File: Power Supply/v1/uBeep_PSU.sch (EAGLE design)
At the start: 1 part, among them U1 RAC10-12DK/277

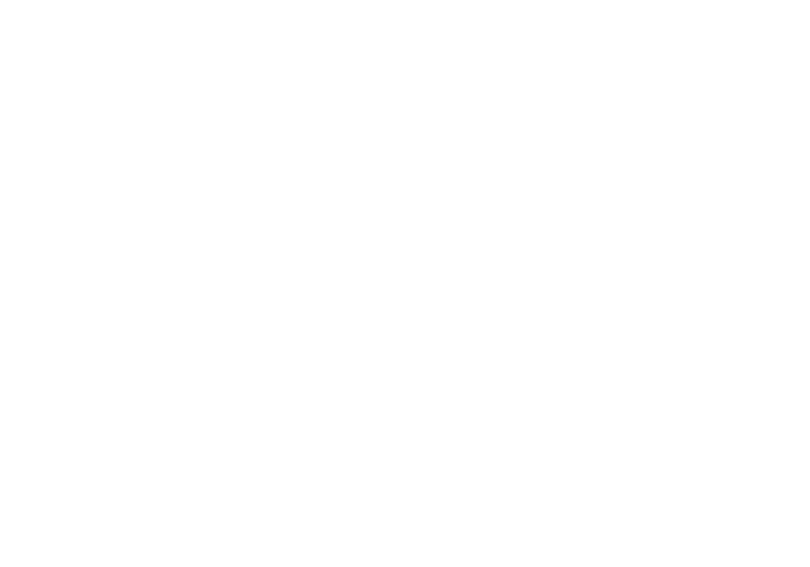
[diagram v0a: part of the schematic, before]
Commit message: Added AC input
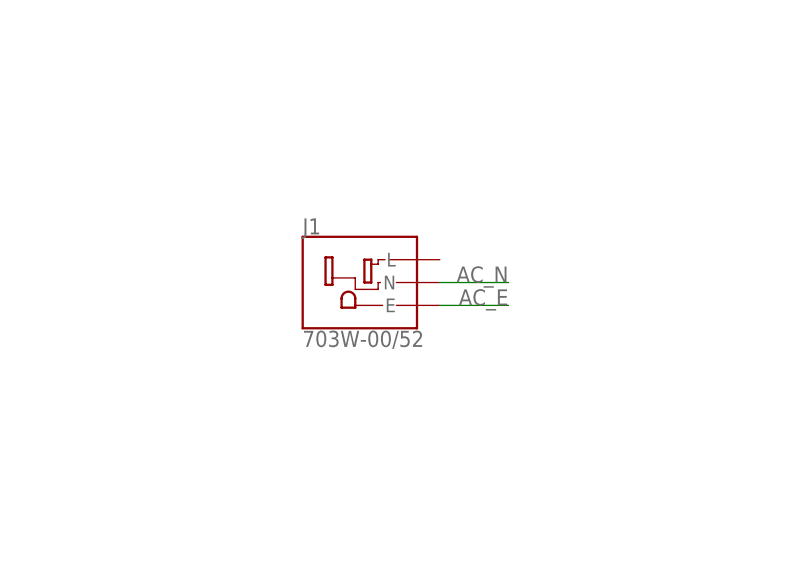
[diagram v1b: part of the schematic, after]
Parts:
- added J1: 703W-00/52, roomready:703W-00/52
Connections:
- new net AC_E: J1.E
- net AC_N: now also J1.N
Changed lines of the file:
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@@
 <part name="U1" library="roomready" library_urn="urn:adsk.eagle:library:9911636" deviceset="RAC10-DK/277" device="" package3d_urn="urn:adsk.eagle:package:12501210/3" value="RAC10-12DK/277"/>
 <part name="GND1" library="supply1" library_urn="urn:adsk.eagle:library:371" deviceset="GND" device=""/>
+<part name="J1" library="roomready" library_urn="urn:adsk.eagle:library:9911636" deviceset="703W-00/52" device="" package3d_urn="urn:adsk.eagle:package:12502137/10"/>
 </parts>
 <sheets>
@@
 <instance part="GND1" gate="1" x="203.2" y="215.9" smashed="yes">
 <attribute name="VALUE" x="200.66" y="213.36" size="1.778" layer="96"/>
+</instance>
+<instance part="J1" gate="G$1" x="76.2" y="218.44" smashed="yes">
+<attribute name="NAME" x="68.564" y="223.786" size="1.7808" layer="95"/>
+<attribute name="VALUE" x="68.5469" y="211.2867" size="1.783790625" layer="96"/>
 </instance>
 </instances>
@@
 <label x="157.48" y="218.44" size="1.778" layer="95"/>
 </segment>
+<segment>
+<pinref part="J1" gate="G$1" pin="N"/>
+<wire x1="83.82" y1="218.44" x2="91.44" y2="218.44" width="0.1524" layer="91"/>
+<label x="91.44" y="218.44" size="1.778" layer="95" rot="MR0"/>
+</segment>
 </net>
+<net name="AC_E" class="0">
+<segment>
+<pinref part="J1" gate="G$1" pin="E"/>
+<wire x1="83.82" y1="215.9" x2="91.44" y2="215.9" width="0.1524" layer="91"/>
+<label x="91.44" y="215.9" size="1.778" layer="95" rot="MR0"/>
+</segment>
+</net>

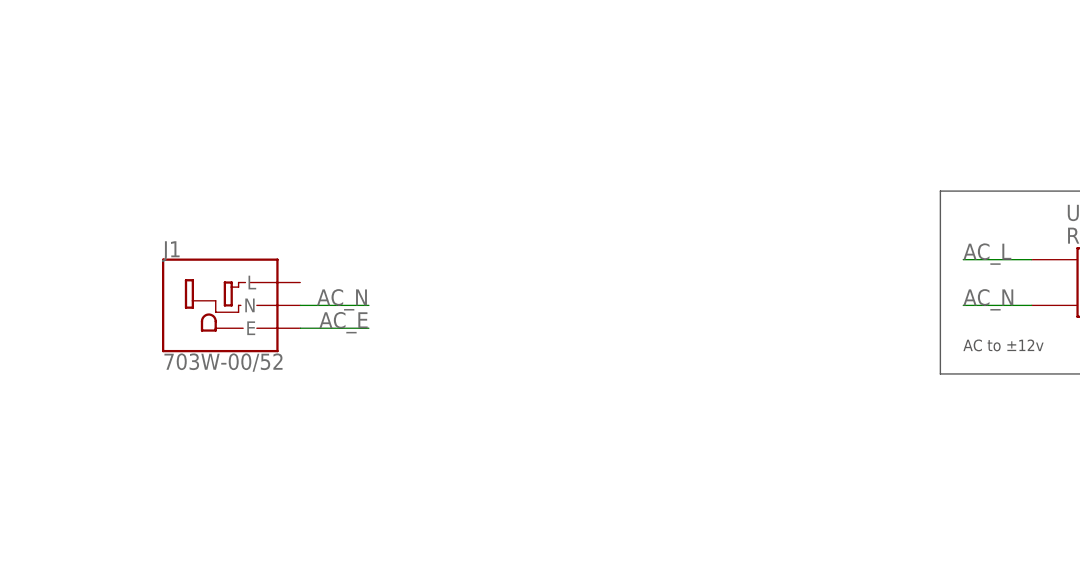
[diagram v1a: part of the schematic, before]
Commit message: Add fuse holder
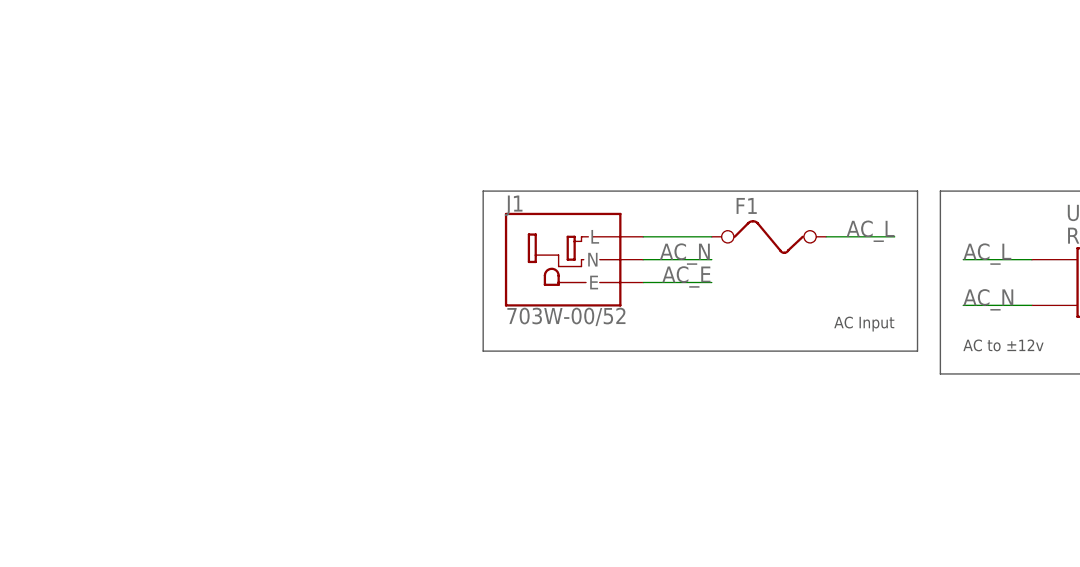
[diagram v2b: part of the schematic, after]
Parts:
- added F1: (no value), roomready:0PTF0075P
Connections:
- new net N$1: F1.1, J1.L
- net AC_L: now also F1.2
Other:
- note added: "AC Input"
- moved on the sheet: J1
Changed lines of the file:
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@@
 <part name="GND1" library="supply1" library_urn="urn:adsk.eagle:library:371" deviceset="GND" device=""/>
 <part name="J1" library="roomready" library_urn="urn:adsk.eagle:library:9911636" deviceset="703W-00/52" device="" package3d_urn="urn:adsk.eagle:package:12502137/10"/>
+<part name="F1" library="roomready" library_urn="urn:adsk.eagle:library:9911636" deviceset="0PTF0075P" device="" package3d_urn="urn:adsk.eagle:package:7587831/2"/>
 </parts>
 <sheets>
@@
 <wire x1="208.28" y1="231.14" x2="154.94" y2="231.14" width="0.1524" layer="97"/>
 <text x="157.48" y="213.36" size="1.27" layer="97">AC to ±12v</text>
+<wire x1="152.4" y1="231.14" x2="104.14" y2="231.14" width="0.1524" layer="97"/>
+<wire x1="104.14" y1="231.14" x2="104.14" y2="213.36" width="0.1524" layer="97"/>
+<wire x1="104.14" y1="213.36" x2="152.4" y2="213.36" width="0.1524" layer="97"/>
+<wire x1="152.4" y1="213.36" x2="152.4" y2="231.14" width="0.1524" layer="97"/>
+<text x="149.86" y="215.9" size="1.27" layer="97" rot="MR0">AC Input</text>
 </plain>
 <instances>
@@
 <attribute name="VALUE" x="200.66" y="213.36" size="1.778" layer="96"/>
 </instance>
-<instance part="J1" gate="G$1" x="76.2" y="218.44" smashed="yes">
-<attribute name="NAME" x="68.564" y="223.786" size="1.7808" layer="95"/>
-<attribute name="VALUE" x="68.5469" y="211.2867" size="1.783790625" layer="96"/>
+<instance part="J1" gate="G$1" x="114.3" y="223.52" smashed="yes">
+<attribute name="NAME" x="106.664" y="228.866" size="1.7808" layer="95"/>
+<attribute name="VALUE" x="106.6469" y="216.3667" size="1.783790625" layer="96"/>
+</instance>
+<instance part="F1" gate="G$1" x="137.16" y="226.06" smashed="yes">
+<attribute name="NAME" x="132.08" y="228.6" size="1.778" layer="95"/>
+<attribute name="VALUE" x="132.08" y="222.25" size="1.778" layer="96"/>
 </instance>
 </instances>
@@
 <label x="157.48" y="223.52" size="1.778" layer="95"/>
 </segment>
+<segment>
+<pinref part="F1" gate="G$1" pin="2"/>
+<wire x1="142.24" y1="226.06" x2="149.86" y2="226.06" width="0.1524" layer="91"/>
+<label x="149.86" y="226.06" size="1.778" layer="95" rot="MR0"/>
+</segment>
 </net>
 <net name="AC_N" class="0">
@@
 <segment>
 <pinref part="J1" gate="G$1" pin="N"/>
-<wire x1="83.82" y1="218.44" x2="91.44" y2="218.44" width="0.1524" layer="91"/>
-<label x="91.44" y="218.44" size="1.778" layer="95" rot="MR0"/>
+<wire x1="121.92" y1="223.52" x2="129.54" y2="223.52" width="0.1524" layer="91"/>
+<label x="129.54" y="223.52" size="1.778" layer="95" rot="MR0"/>
 </segment>
 </net>
@@
 <segment>
 <pinref part="J1" gate="G$1" pin="E"/>
-<wire x1="83.82" y1="215.9" x2="91.44" y2="215.9" width="0.1524" layer="91"/>
-<label x="91.44" y="215.9" size="1.778" layer="95" rot="MR0"/>
+<wire x1="121.92" y1="220.98" x2="129.54" y2="220.98" width="0.1524" layer="91"/>
+<label x="129.54" y="220.98" size="1.778" layer="95" rot="MR0"/>
 </segment>
 </net>
+<net name="N$1" class="0">
+<segment>
+<pinref part="J1" gate="G$1" pin="L"/>
+<pinref part="F1" gate="G$1" pin="1"/>
+<wire x1="121.92" y1="226.06" x2="129.54" y2="226.06" width="0.1524" layer="91"/>
+</segment>
+</net>
